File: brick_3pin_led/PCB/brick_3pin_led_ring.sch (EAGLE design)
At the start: 27 parts

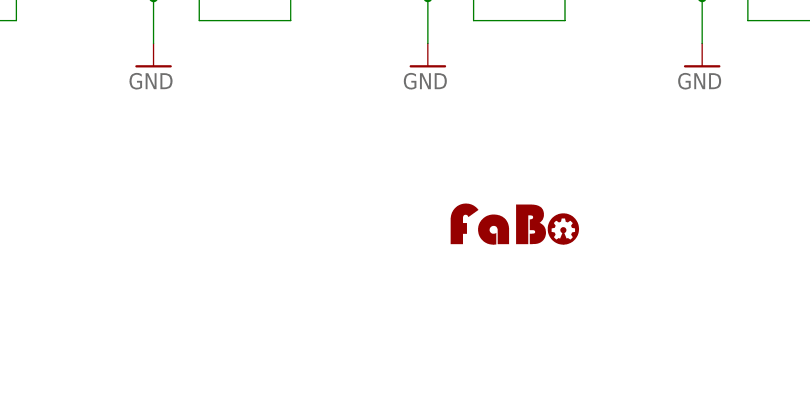
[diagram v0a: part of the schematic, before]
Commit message: change screwhole brick_3pin_led_ring
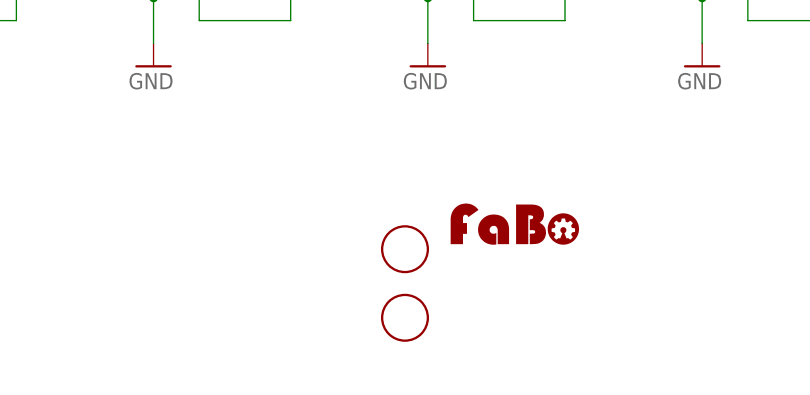
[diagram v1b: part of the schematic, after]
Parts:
- added U$16, U$17: (no value), GClue:SCREW-PAD-3MM
- U$15: device GClue:LOGO_OSHW_T-S -> GClue:LOGO_OSHW_T-M
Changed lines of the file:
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@@
 <part name="GND12" library="GClue" deviceset="GND" device=""/>
 <part name="GND13" library="GClue" deviceset="GND" device=""/>
-<part name="U$15" library="GClue" deviceset="LOGO_OSHW_T" device="-S"/>
+<part name="U$16" library="GClue" deviceset="SCREW-PAD" device="-3MM"/>
+<part name="U$17" library="GClue" deviceset="SCREW-PAD" device="-3MM"/>
+<part name="U$15" library="GClue" deviceset="LOGO_OSHW_T" device="-M"/>
 </parts>
 <sheets>
@@
 <instance part="GND12" gate="GND" x="190.5" y="40.64"/>
 <instance part="GND13" gate="GND" x="220.98" y="40.64"/>
+<instance part="U$16" gate="G$1" x="157.48" y="17.78"/>
+<instance part="U$17" gate="G$1" x="157.48" y="10.16"/>
 <instance part="U$15" gate="G$1" x="208.28" y="12.7"/>
 </instances>

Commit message: change revision 1.0 brick_analog
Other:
- note added: "1.0"
- note removed: "Beta2"
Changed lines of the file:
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@@
 <sheet>
 <plain>
-<text x="251.46" y="5.08" size="2.54" layer="94" align="bottom-center">Beta2</text>
+<text x="251.46" y="5.08" size="2.54" layer="94" align="bottom-center">1.0</text>
 </plain>
 <instances>

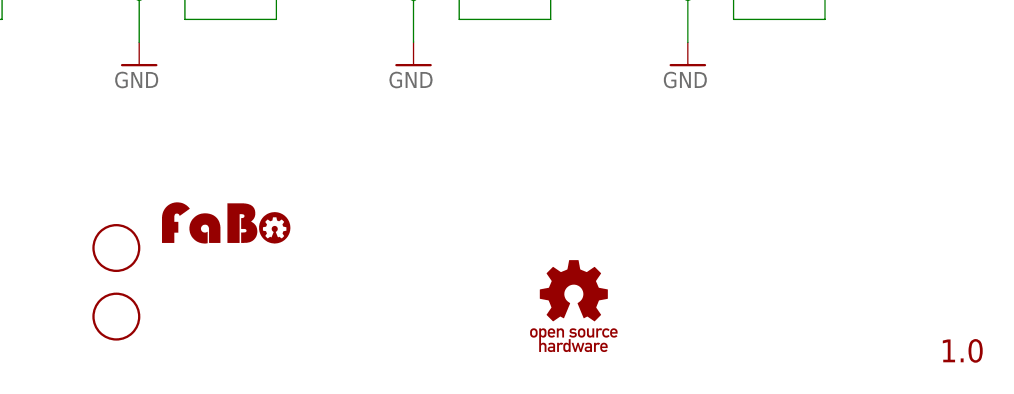
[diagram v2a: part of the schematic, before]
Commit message: change revision 1.0.0  brick_3pin_led
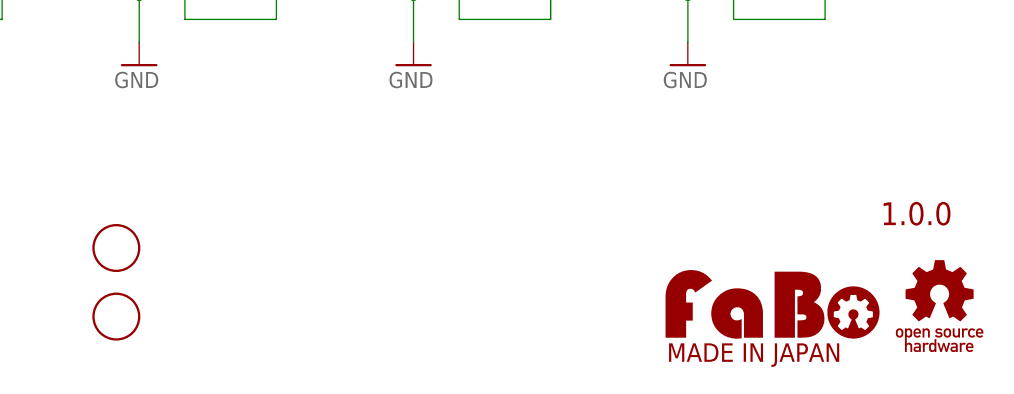
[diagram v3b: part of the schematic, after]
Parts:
- U$14: device FaBo:LOGO_FABO-M -> FaBo-etc:LOGO_FABO-M
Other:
- note added: "1.0.0"
- note removed: "1.0"
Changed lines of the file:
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@@
 <?xml version="1.0" encoding="utf-8"?>
 <!DOCTYPE eagle SYSTEM "eagle.dtd">
-<eagle version="7.3.0">
+<eagle version="7.4.0">
 <drawing>
 <settings>
@@
 <setting verticaltext="up"/>
 </settings>
-<grid distance="0.1" unitdist="inch" unit="inch" style="lines" multiple="1" display="no" altdistance="0.01" altunitdist="inch" altunit="inch"/>
+<grid distance="0.1" unitdist="inch" unit="inch" style="lines" multiple="1" display="yes" altdistance="0.01" altunitdist="inch" altunit="inch"/>
 <layers>
 <layer number="1" name="Top" color="4" fill="1" visible="no" active="no"/>
@@
 <layer number="154" name="FabDoc2" color="2" fill="1" visible="no" active="no"/>
 <layer number="155" name="FabDoc3" color="7" fill="15" visible="no" active="no"/>
+<layer number="160" name="O_Dim" color="12" fill="11" visible="no" active="yes"/>
 <layer number="199" name="Contour" color="7" fill="1" visible="yes" active="yes"/>
 <layer number="200" name="200bmp" color="1" fill="10" visible="yes" active="yes"/>
@@
 </classes>
 <parts>
-<part name="U$1" library="GClue" deviceset="A4L-LOC" device=""/>
 <part name="U$2" library="GClue-LED" deviceset="WS2818B" device=""/>
 <part name="U$3" library="GClue-LED" deviceset="WS2818B" device=""/>
@@
 <part name="C5" library="GClue" deviceset="CAP" device="-EIA0603" value="0.1uF"/>
 <part name="C6" library="GClue" deviceset="CAP" device="-EIA0603" value="0.1uF"/>
-<part name="U$14" library="FaBo" deviceset="LOGO_FABO" device="-M"/>
 <part name="SUPPLY4" library="GClue" deviceset="5V" device=""/>
 <part name="GND4" library="GClue" deviceset="GND" device=""/>
@@
 <part name="U$17" library="GClue" deviceset="SCREW-PAD" device="-3MM"/>
 <part name="U$15" library="GClue" deviceset="LOGO_OSHW_T" device="-M"/>
+<part name="U$1" library="FaBo-etc" deviceset="A4L-LOC" device=""/>
+<part name="U$14" library="FaBo-etc" deviceset="LOGO_FABO" device="-M"/>
 </parts>
 <sheets>
 <sheet>
 <plain>
-<text x="251.46" y="5.08" size="2.54" layer="94" align="bottom-center">1.0</text>
+<text x="246.38" y="20.32" size="2.54" layer="94" align="bottom-center">1.0.0</text>
 </plain>
 <instances>
-<instance part="U$1" gate="G$1" x="0" y="0"/>
 <instance part="U$2" gate="G$1" x="81.28" y="121.92" rot="R270"/>
 <instance part="U$3" gate="G$1" x="111.76" y="121.92" rot="R270"/>
@@
 <instance part="C5" gate="G$1" x="190.5" y="121.92" rot="R180"/>
 <instance part="C6" gate="G$1" x="220.98" y="121.92" rot="R180"/>
-<instance part="U$14" gate="G$1" x="162.56" y="22.86"/>
 <instance part="SUPPLY4" gate="5V" x="129.54" y="142.24"/>
 <instance part="GND4" gate="GND" x="129.54" y="104.14"/>
@@
 <instance part="U$16" gate="G$1" x="157.48" y="17.78"/>
 <instance part="U$17" gate="G$1" x="157.48" y="10.16"/>
-<instance part="U$15" gate="G$1" x="208.28" y="12.7"/>
+<instance part="U$15" gate="G$1" x="248.92" y="12.7"/>
+<instance part="U$1" gate="G$1" x="0" y="0"/>
+<instance part="U$14" gate="G$1" x="218.44" y="5.08"/>
 </instances>
 <busses>
